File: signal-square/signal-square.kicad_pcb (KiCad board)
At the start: 2 copper layers, 26 x 17.5 mm, 14 parts, among them SW1 SW_Push_DPDT

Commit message: Fix package.
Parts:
- D2: footprint Package_TO_SOT_SMD:SOT-323_SC-70_Handsoldering -> Package_TO_SOT_SMD:SOT-23_Handsoldering
- moved D2 0.60 mm to (103.3, 32.1)
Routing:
- net GND: vias 0 -> 3

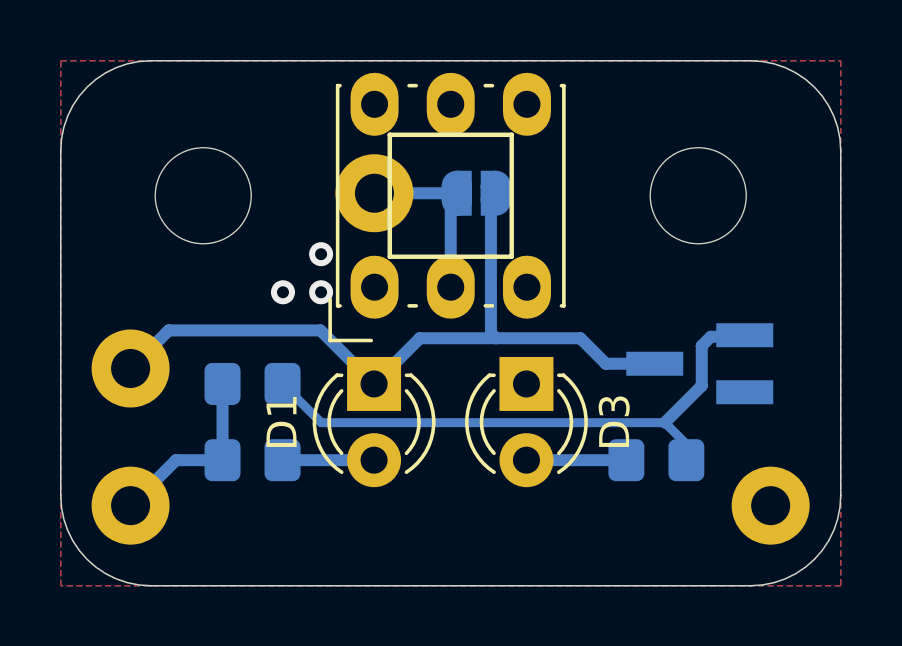
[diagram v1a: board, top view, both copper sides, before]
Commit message: Signal: switch diodes.
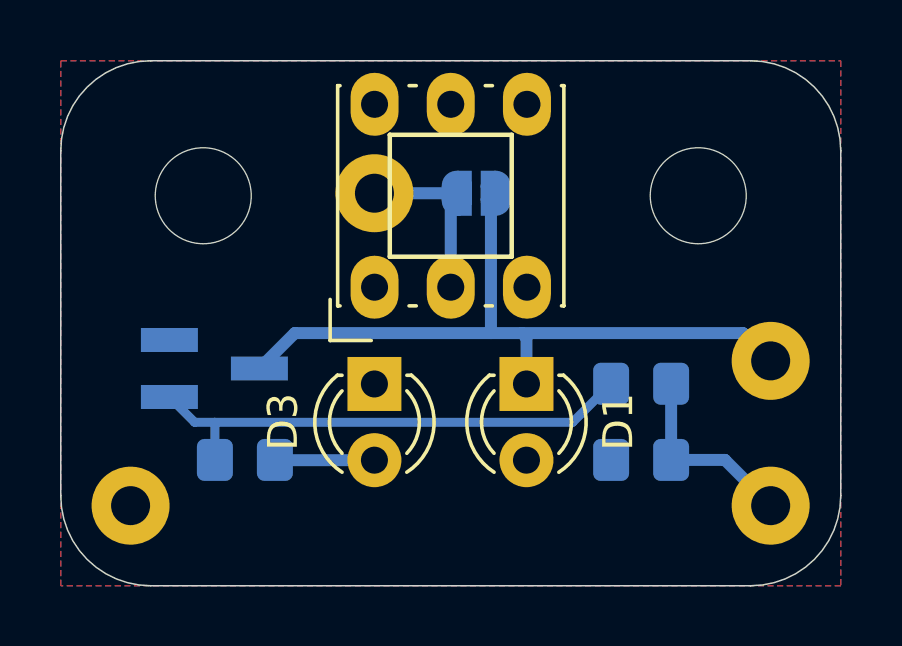
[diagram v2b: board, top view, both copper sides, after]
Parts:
- moved CINPUT1 21.3 mm to (105.7, 32.0)
- moved CGND1 21.3 mm to (84.3, 36.8)
- moved CVCC1 21.3 mm to (105.7, 36.8)
- moved D2 16.2 mm to (87.1, 32.3), turned to 0 degrees
- moved R3 13.7 mm to (88.1, 35.3), turned to 0 degrees
- moved R1 13.0 mm to (101.3, 35.3), turned to 180 degrees
- moved R2 13.0 mm to (101.3, 32.8), turned to 180 degrees
- moved D1 5.08 mm to (97.5, 32.8)
- moved D3 5.07 mm to (92.5, 32.8)
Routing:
- net Net-(D1-Pad2): track 3.05 -> 0.00 mm
- net Net-(D2-Pad1): track 19.6 -> 16.9 mm
- net GND: vias 3 -> 0
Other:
- board text added: "Návěstidlo Se-sq v2.0 JH 2021"
- board text removed: "Návěstidlo Se-sq v1.0 JH 2021"

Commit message: Add missing wire.
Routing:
- net Net-(D1-Pad2): track 0.00 -> 2.83 mm
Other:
- board text added: "GO"
- board text added: "Návěstidlo Se-sq v2.1 JH 2022"
- board text added: "STOP"
- board text removed: "Návěstidlo Se-sq v2.0 JH 2021"
